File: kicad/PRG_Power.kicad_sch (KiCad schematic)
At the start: 18 parts, among them IC2 4049

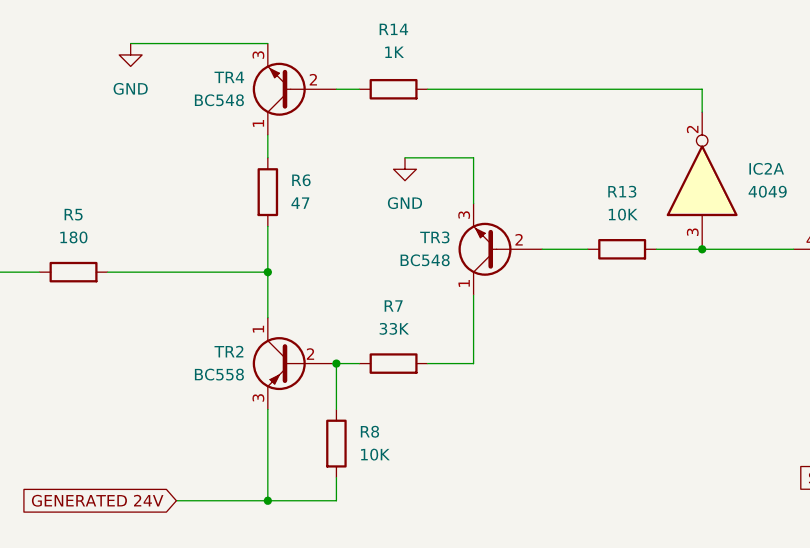
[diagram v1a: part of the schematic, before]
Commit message: Kicad 9 and Docs
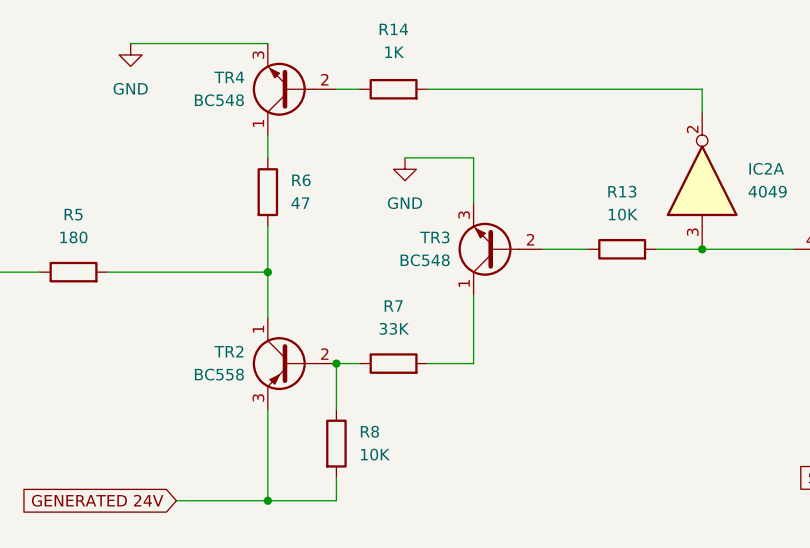
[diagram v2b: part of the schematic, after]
